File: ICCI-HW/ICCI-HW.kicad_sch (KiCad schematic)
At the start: 0 parts

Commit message: schematic V1.0
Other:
- sheet AUX + Peripherals ports: added 3V_BAT, SCL0, SDA0; removed ~{SAFEBOOT}
- sheet BATT + POWER ports: added none; removed VBUS
- sheet ESP ports: added 3V_BAT; removed VBUS, ~{SAFEBOOT}
- sheet USB ports: added none; removed VBUS
- note added: "# TODO - check"
- note removed: "# TODO - Testpoints - MH - controllare"
- note removed: "Completed: Check:"
- note removed: "Completed: OK Check:"
- note removed: "TPS NON DISPONIBILE ISET"

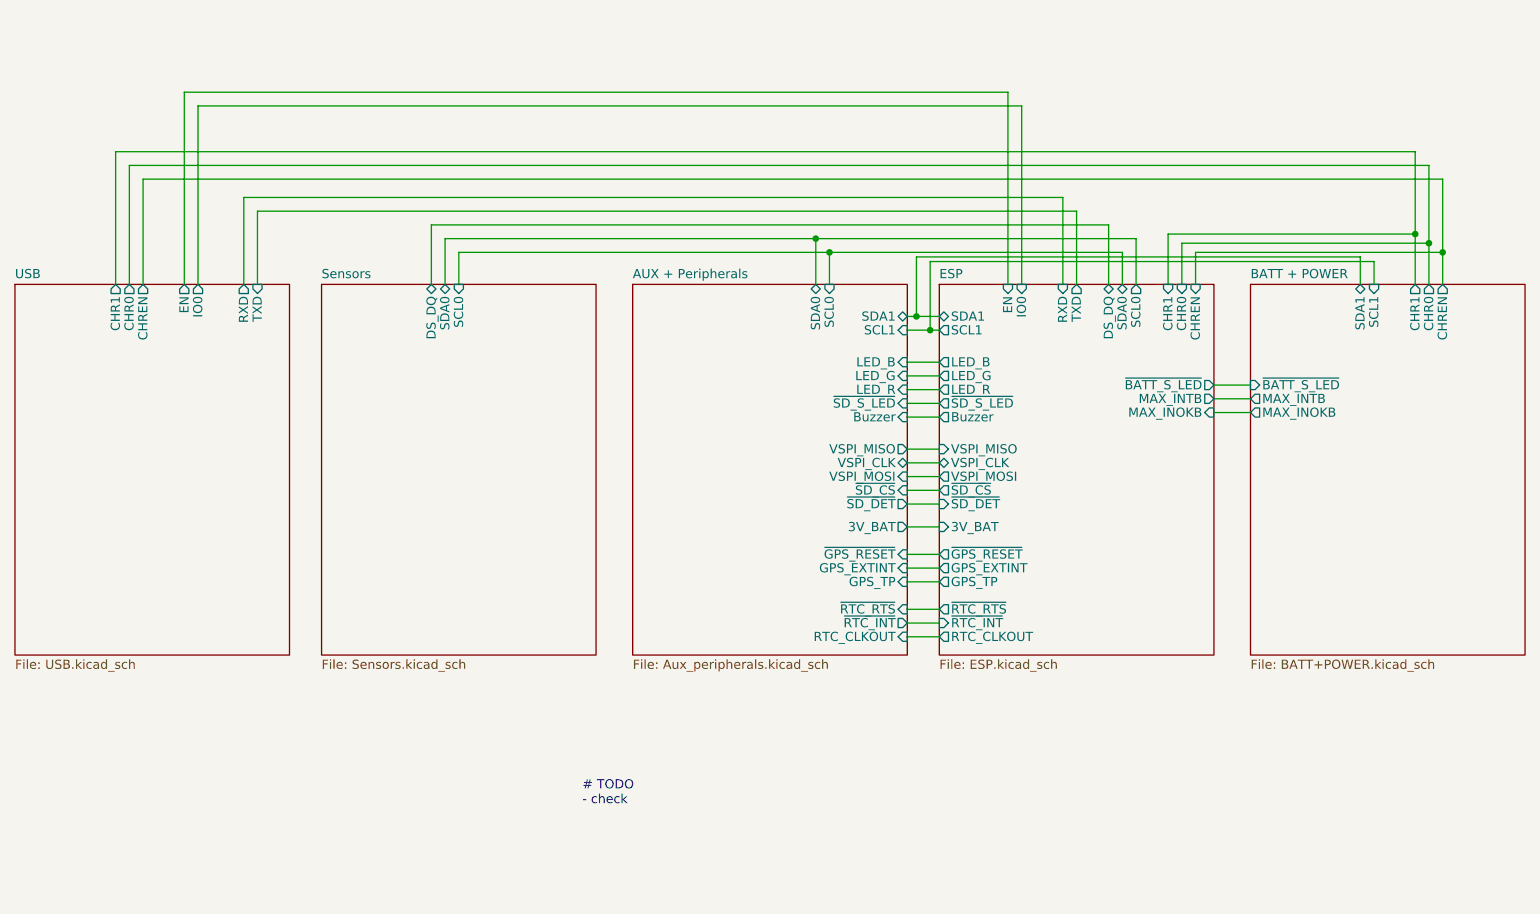
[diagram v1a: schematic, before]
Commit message: footprint assigned
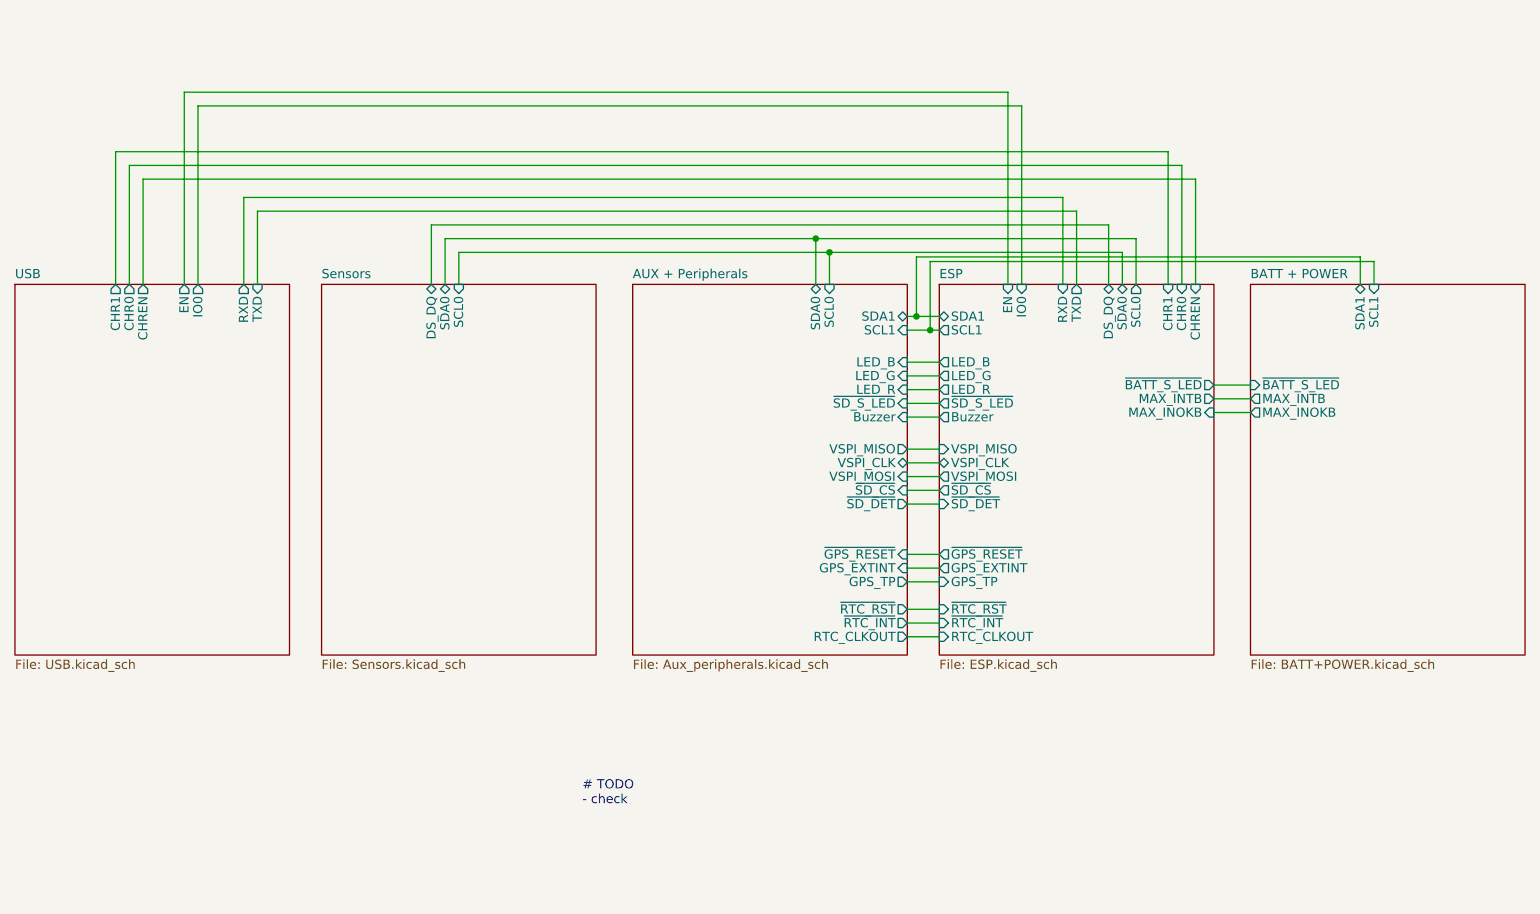
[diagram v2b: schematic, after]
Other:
- sheet AUX + Peripherals ports: added ~{RTC_RST}; removed 3V_BAT, ~{RTC_RTS}
- sheet BATT + POWER ports: added none; removed CHR0, CHR1, CHREN
- sheet ESP ports: added ~{RTC_RST}; removed 3V_BAT, ~{RTC_RTS}

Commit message: fw: updates
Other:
- sheet AUX + Peripherals ports: added ~{GPS_EN}; removed none
- sheet ESP ports: added ~{GPS_EN}; removed none
- note added: "# TODO - USB current not clear - check footprint - check"
- note removed: "# TODO - check"

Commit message: hw: updates
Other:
- note removed: "# TODO - USB current not clear - check footprint - check"
- company: tollsimy -> Simone Tollardo

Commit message: hw: updates
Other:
- note added: "- solve small errors on DRC"
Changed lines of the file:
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@@
     (stroke (width 0) (type default) (color 0 0 0 0))
+  )
+  (text "- solve small errors on DRC" (at 112.395 144.145 0)
+    (effects (font (size 3 3)) (justify left bottom))
   )
   (sheet (at 131.445 69.85) (size 38.1 51.435) (fields_autoplaced)
